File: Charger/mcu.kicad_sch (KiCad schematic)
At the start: 15 parts, among them U23 RaspberryPi_Pico, U24 CD4051B

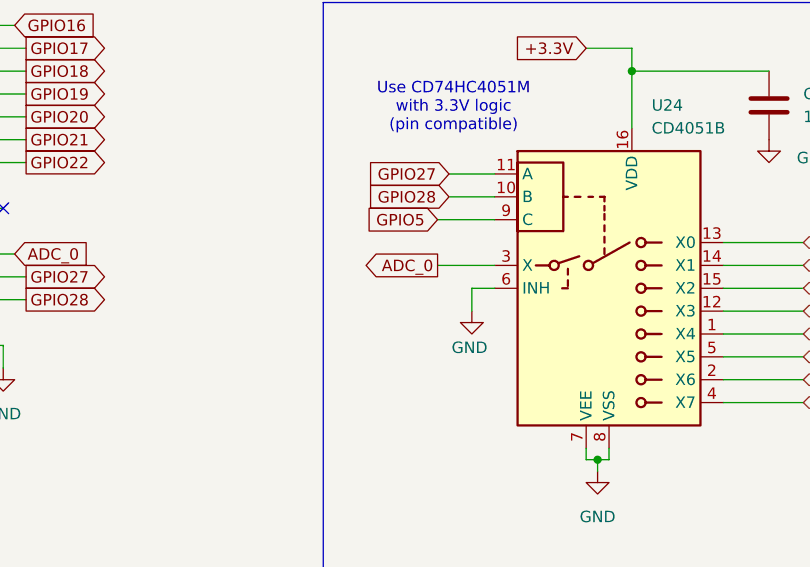
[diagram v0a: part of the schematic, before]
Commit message: up
zmienione kilka sciezek, dodane przelotki do masy i rezystor do adc
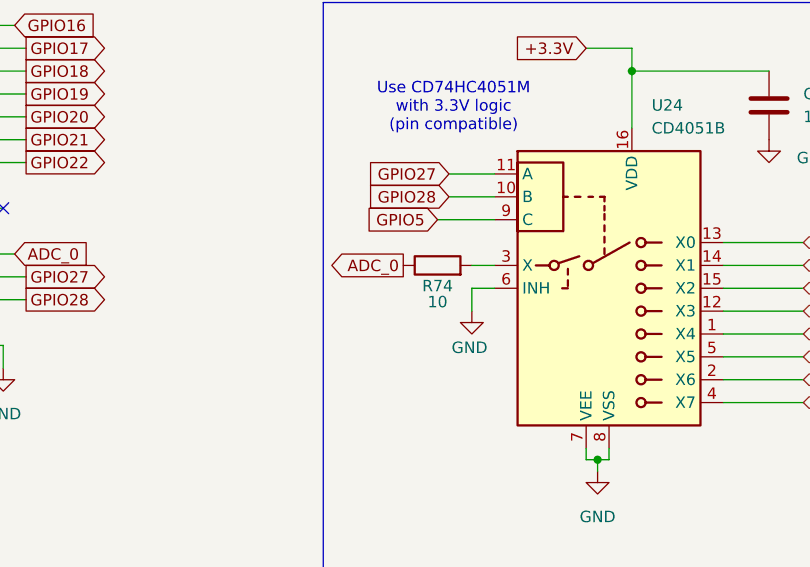
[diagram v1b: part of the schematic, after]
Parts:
- added R74: 10, Resistor_SMD:R_0805_2012Metric_Pad1.20x1.40mm_HandSolder, symbol Device:R
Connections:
- net ADC_0: now also R74.1; no longer U24.3 (X)
- new net: R74.2, U24.3 (X)
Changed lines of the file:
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@@
+	(wire
+		(pts
+			(xy 226.06 102.87) (xy 228.6 102.87)
+		)
+		(stroke
+			(width 0)
+			(type default)
+		)
+	)
 	(wire
 		(pts
@@
 		(pts
 			(xy 123.19 81.28) (xy 125.73 81.28)
-		)
-		(stroke
-			(width 0)
-			(type default)
-		)
-	)
-	(wire
-		(pts
-			(xy 222.25 102.87) (xy 228.6 102.87)
 		)
 		(stroke
@@
 	(global_label "ADC_0"
 		(shape output)
-		(at 222.25 102.87 180)
-		(fields_autoplaced yes)
-		(effects
-			(font
-				(size 1.27 1.27)
-			)
-			(justify right)
-		)
-		(property "Intersheetrefs" "${INTERSHEET_REFS}"
-			(at 213.4591 102.87 0)
+		(at 218.44 102.87 180)
+		(fields_autoplaced yes)
+		(effects
+			(font
+				(size 1.27 1.27)
+			)
+			(justify right)
+		)
+		(property "Intersheetrefs" "${INTERSHEET_REFS}"
+			(at 209.6491 102.87 0)
 			(effects
 				(font
@@
 					(unit 1)
 				)
+			)
+		)
+	)
+	(symbol
+		(lib_id "Device:R")
+		(at 222.25 102.87 90)
+		(unit 1)
+		(exclude_from_sim no)
+		(in_bom yes)
+		(on_board yes)
+		(dnp no)
+		(property "Reference" "R74"
+			(at 222.25 105.156 90)
+			(effects
+				(font
+					(size 1.27 1.27)
+				)
+			)
+		)
+		(property "Value" "10"
+			(at 222.25 106.934 90)
+			(effects
+				(font
+					(size 1.27 1.27)
+				)
+			)
+		)
+		(property "Footprint" "Resistor_SMD:R_0805_2012Metric_Pad1.20x1.40mm_HandSolder"
+			(at 222.25 104.648 90)
+			(effects
+				(font
+					(size 1.27 1.27)
+				)
+				(hide yes)
+			)
+		)
+		(property "Datasheet" "~"
+			(at 222.25 102.87 0)
+			(effects
+				(font
+					(size 1.27 1.27)
+				)
+				(hide yes)
+			)
+		)
+		(property "Description" "Resistor"
+			(at 222.25 102.87 0)
+			(effects
+				(font
+					(size 1.27 1.27)
+				)
+				(hide yes)
+			)
+		)
+		(pin "1"
+		)
+		(pin "2"
+		)
+		(instances
+			(project "Charger"
+				(path "/f0501846-9b00-4ec1-8596-952177c35a04/8abca69a-4cf1-41f6-b583-47d31555f535"
+					(reference "R74")
+					(unit 1)
+				)
